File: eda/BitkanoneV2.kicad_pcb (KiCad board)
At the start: 2 copper layers, 0 parts

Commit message: WS2812B grid finished
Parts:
- added C401: 220u, Capacitor_SMD:CP_Elec_6.3x5.3, F.Cu at (273.8, 116.9)
- added C402: 220u, Capacitor_SMD:CP_Elec_6.3x5.3, F.Cu at (273.8, 109.7)
- added C900: 220u, Capacitor_SMD:CP_Elec_6.3x5.3, F.Cu at (53.0, 125.0)
- added C901: 100nF, Capacitor_SMD:C_0603_1608Metric, F.Cu at (32.0, 27.0)
- added C902: 100nF, Capacitor_SMD:C_0603_1608Metric, F.Cu at (46.0, 27.0)
- added C903: 100nF, Capacitor_SMD:C_0603_1608Metric, F.Cu at (60.0, 27.0)
- added C904: 100nF, Capacitor_SMD:C_0603_1608Metric, F.Cu at (74.0, 27.0)
- added C905: 100nF, Capacitor_SMD:C_0603_1608Metric, F.Cu at (88.0, 27.0)
- added C906: 100nF, Capacitor_SMD:C_0603_1608Metric, F.Cu at (102.0, 27.0)
- added C907: 100nF, Capacitor_SMD:C_0603_1608Metric, F.Cu at (116.0, 27.0)
- added C908: 100nF, Capacitor_SMD:C_0603_1608Metric, F.Cu at (32.0, 41.0)
- added C909: 100nF, Capacitor_SMD:C_0603_1608Metric, F.Cu at (46.0, 41.0)
- added C910: 100nF, Capacitor_SMD:C_0603_1608Metric, F.Cu at (60.0, 41.0)
- added C911: 100nF, Capacitor_SMD:C_0603_1608Metric, F.Cu at (74.0, 41.0)
- added C912: 100nF, Capacitor_SMD:C_0603_1608Metric, F.Cu at (88.0, 41.0)
- added C913: 100nF, Capacitor_SMD:C_0603_1608Metric, F.Cu at (102.0, 41.0)
- added C914: 100nF, Capacitor_SMD:C_0603_1608Metric, F.Cu at (116.0, 41.0)
- added C915: 100nF, Capacitor_SMD:C_0603_1608Metric, F.Cu at (32.0, 55.0)
- added C916: 100nF, Capacitor_SMD:C_0603_1608Metric, F.Cu at (46.0, 55.0)
- added C917: 100nF, Capacitor_SMD:C_0603_1608Metric, F.Cu at (60.0, 55.0)
- added C918: 100nF, Capacitor_SMD:C_0603_1608Metric, F.Cu at (74.0, 55.0)
- added C919: 100nF, Capacitor_SMD:C_0603_1608Metric, F.Cu at (81.1, 48.6)
- added C920: 100nF, Capacitor_SMD:C_0603_1608Metric, F.Cu at (102.0, 55.0)
- added C921: 100nF, Capacitor_SMD:C_0603_1608Metric, F.Cu at (116.0, 55.0)
- added C922: 100nF, Capacitor_SMD:C_0603_1608Metric, F.Cu at (32.0, 69.0)
- added C923: 100nF, Capacitor_SMD:C_0603_1608Metric, F.Cu at (46.0, 69.0)
- added C924: 100nF, Capacitor_SMD:C_0603_1608Metric, F.Cu at (60.0, 69.0)
- added C925: 100nF, Capacitor_SMD:C_0603_1608Metric, F.Cu at (74.0, 69.0)
- added C926: 100nF, Capacitor_SMD:C_0603_1608Metric, F.Cu at (88.0, 69.0)
- added C927: 100nF, Capacitor_SMD:C_0603_1608Metric, F.Cu at (102.0, 69.0)
- added C928: 100nF, Capacitor_SMD:C_0603_1608Metric, F.Cu at (116.0, 69.0)
- added C929: 100nF, Capacitor_SMD:C_0603_1608Metric, F.Cu at (32.0, 83.0)
- added C930: 100nF, Capacitor_SMD:C_0603_1608Metric, F.Cu at (46.0, 83.0)
- added C931: 100nF, Capacitor_SMD:C_0603_1608Metric, F.Cu at (60.0, 83.0)
- added C932: 100nF, Capacitor_SMD:C_0603_1608Metric, F.Cu at (74.0, 83.0)
- added C933: 100nF, Capacitor_SMD:C_0603_1608Metric, F.Cu at (88.0, 83.0)
- added C934: 100nF, Capacitor_SMD:C_0603_1608Metric, F.Cu at (102.0, 83.0)
- added C935: 100nF, Capacitor_SMD:C_0603_1608Metric, F.Cu at (116.0, 83.0)
- added C936: 100nF, Capacitor_SMD:C_0603_1608Metric, F.Cu at (32.0, 97.0)
- added C937: 100nF, Capacitor_SMD:C_0603_1608Metric, F.Cu at (46.3, 97.0)
- added C938: 100nF, Capacitor_SMD:C_0603_1608Metric, F.Cu at (60.0, 97.0)
- added C939: 100nF, Capacitor_SMD:C_0603_1608Metric, F.Cu at (74.0, 97.0)
- added C940: 100nF, Capacitor_SMD:C_0603_1608Metric, F.Cu at (88.0, 97.0)
- added C941: 100nF, Capacitor_SMD:C_0603_1608Metric, F.Cu at (102.0, 97.0)
- added C942: 100nF, Capacitor_SMD:C_0603_1608Metric, F.Cu at (116.0, 97.0)
- added C943: 100nF, Capacitor_SMD:C_0603_1608Metric, F.Cu at (32.0, 111.0)
- added C944: 100nF, Capacitor_SMD:C_0603_1608Metric, F.Cu at (46.3, 111.0)
- added C945: 100nF, Capacitor_SMD:C_0603_1608Metric, F.Cu at (60.0, 111.0)
- added C946: 100nF, Capacitor_SMD:C_0603_1608Metric, F.Cu at (74.0, 111.0)
- added C947: 100nF, Capacitor_SMD:C_0603_1608Metric, F.Cu at (88.0, 111.0)
- added C948: 100nF, Capacitor_SMD:C_0603_1608Metric, F.Cu at (102.0, 111.0)
- added C949: 100nF, Capacitor_SMD:C_0603_1608Metric, F.Cu at (116.0, 111.0)
- added D901: WS2812B, LED_SMD:LED_WS2812B_PLCC4_5.0x5.0mm_P3.2mm, F.Cu at (27.0, 27.0)
- added D902: WS2812B, LED_SMD:LED_WS2812B_PLCC4_5.0x5.0mm_P3.2mm, F.Cu at (41.0, 27.0)
- added D903: WS2812B, LED_SMD:LED_WS2812B_PLCC4_5.0x5.0mm_P3.2mm, F.Cu at (55.0, 27.0)
- added D904: WS2812B, LED_SMD:LED_WS2812B_PLCC4_5.0x5.0mm_P3.2mm, F.Cu at (69.0, 27.0)
- added D905: WS2812B, LED_SMD:LED_WS2812B_PLCC4_5.0x5.0mm_P3.2mm, F.Cu at (83.0, 27.0)
- added D906: WS2812B, LED_SMD:LED_WS2812B_PLCC4_5.0x5.0mm_P3.2mm, F.Cu at (97.0, 27.0)
- added D907: WS2812B, LED_SMD:LED_WS2812B_PLCC4_5.0x5.0mm_P3.2mm, F.Cu at (111.0, 27.0)
- added D908: WS2812B, LED_SMD:LED_WS2812B_PLCC4_5.0x5.0mm_P3.2mm, F.Cu at (27.0, 41.0)
- added D909: WS2812B, LED_SMD:LED_WS2812B_PLCC4_5.0x5.0mm_P3.2mm, F.Cu at (41.0, 41.0)
- added D910: WS2812B, LED_SMD:LED_WS2812B_PLCC4_5.0x5.0mm_P3.2mm, F.Cu at (55.0, 41.0)
- added D911: WS2812B, LED_SMD:LED_WS2812B_PLCC4_5.0x5.0mm_P3.2mm, F.Cu at (69.0, 41.0)
- added D912: WS2812B, LED_SMD:LED_WS2812B_PLCC4_5.0x5.0mm_P3.2mm, F.Cu at (83.0, 41.0)
- added D913: WS2812B, LED_SMD:LED_WS2812B_PLCC4_5.0x5.0mm_P3.2mm, F.Cu at (97.0, 41.0)
- added D914: WS2812B, LED_SMD:LED_WS2812B_PLCC4_5.0x5.0mm_P3.2mm, F.Cu at (111.0, 41.0)
- added D915: WS2812B, LED_SMD:LED_WS2812B_PLCC4_5.0x5.0mm_P3.2mm, F.Cu at (27.0, 55.0)
- added D916: WS2812B, LED_SMD:LED_WS2812B_PLCC4_5.0x5.0mm_P3.2mm, F.Cu at (41.0, 55.0)
- added D917: WS2812B, LED_SMD:LED_WS2812B_PLCC4_5.0x5.0mm_P3.2mm, F.Cu at (55.0, 55.0)
- added D918: WS2812B, LED_SMD:LED_WS2812B_PLCC4_5.0x5.0mm_P3.2mm, F.Cu at (69.0, 55.0)
- added D919: WS2812B, LED_SMD:LED_WS2812B_PLCC4_5.0x5.0mm_P3.2mm, F.Cu at (83.0, 55.0)
- added D920: WS2812B, LED_SMD:LED_WS2812B_PLCC4_5.0x5.0mm_P3.2mm, F.Cu at (97.0, 55.0)
- added D921: WS2812B, LED_SMD:LED_WS2812B_PLCC4_5.0x5.0mm_P3.2mm, F.Cu at (111.0, 55.0)
- added D922: WS2812B, LED_SMD:LED_WS2812B_PLCC4_5.0x5.0mm_P3.2mm, F.Cu at (27.0, 69.0)
- added D923: WS2812B, LED_SMD:LED_WS2812B_PLCC4_5.0x5.0mm_P3.2mm, F.Cu at (41.0, 69.0)
- added D924: WS2812B, LED_SMD:LED_WS2812B_PLCC4_5.0x5.0mm_P3.2mm, F.Cu at (55.0, 69.0)
- added D925: WS2812B, LED_SMD:LED_WS2812B_PLCC4_5.0x5.0mm_P3.2mm, F.Cu at (69.0, 69.0)
- added D926: WS2812B, LED_SMD:LED_WS2812B_PLCC4_5.0x5.0mm_P3.2mm, F.Cu at (83.0, 69.0)
- added D927: WS2812B, LED_SMD:LED_WS2812B_PLCC4_5.0x5.0mm_P3.2mm, F.Cu at (97.0, 69.0)
- added D928: WS2812B, LED_SMD:LED_WS2812B_PLCC4_5.0x5.0mm_P3.2mm, F.Cu at (111.0, 69.0)
- added D929: WS2812B, LED_SMD:LED_WS2812B_PLCC4_5.0x5.0mm_P3.2mm, F.Cu at (27.0, 83.0)
- added D930: WS2812B, LED_SMD:LED_WS2812B_PLCC4_5.0x5.0mm_P3.2mm, F.Cu at (41.0, 83.0)
- added D931: WS2812B, LED_SMD:LED_WS2812B_PLCC4_5.0x5.0mm_P3.2mm, F.Cu at (55.0, 83.0)
- added D932: WS2812B, LED_SMD:LED_WS2812B_PLCC4_5.0x5.0mm_P3.2mm, F.Cu at (69.0, 83.0)
- added D933: WS2812B, LED_SMD:LED_WS2812B_PLCC4_5.0x5.0mm_P3.2mm, F.Cu at (83.0, 83.0)
- added D934: WS2812B, LED_SMD:LED_WS2812B_PLCC4_5.0x5.0mm_P3.2mm, F.Cu at (97.0, 83.0)
- added D935: WS2812B, LED_SMD:LED_WS2812B_PLCC4_5.0x5.0mm_P3.2mm, F.Cu at (111.0, 83.0)
- added D936: WS2812B, LED_SMD:LED_WS2812B_PLCC4_5.0x5.0mm_P3.2mm, F.Cu at (27.0, 97.0)
- added D937: WS2812B, LED_SMD:LED_WS2812B_PLCC4_5.0x5.0mm_P3.2mm, F.Cu at (41.0, 97.0)
- added D938: WS2812B, LED_SMD:LED_WS2812B_PLCC4_5.0x5.0mm_P3.2mm, F.Cu at (55.0, 97.0)
- added D939: WS2812B, LED_SMD:LED_WS2812B_PLCC4_5.0x5.0mm_P3.2mm, F.Cu at (69.0, 97.0)
- added D940: WS2812B, LED_SMD:LED_WS2812B_PLCC4_5.0x5.0mm_P3.2mm, F.Cu at (83.0, 97.0)
- added D941: WS2812B, LED_SMD:LED_WS2812B_PLCC4_5.0x5.0mm_P3.2mm, F.Cu at (97.0, 97.0)
- added D942: WS2812B, LED_SMD:LED_WS2812B_PLCC4_5.0x5.0mm_P3.2mm, F.Cu at (111.0, 97.0)
- added D943: WS2812B, LED_SMD:LED_WS2812B_PLCC4_5.0x5.0mm_P3.2mm, F.Cu at (27.0, 111.0)
- added D944: WS2812B, LED_SMD:LED_WS2812B_PLCC4_5.0x5.0mm_P3.2mm, F.Cu at (41.0, 111.0)
- added D945: WS2812B, LED_SMD:LED_WS2812B_PLCC4_5.0x5.0mm_P3.2mm, F.Cu at (55.0, 111.0)
- added D946: WS2812B, LED_SMD:LED_WS2812B_PLCC4_5.0x5.0mm_P3.2mm, F.Cu at (69.0, 111.0)
- added D947: WS2812B, LED_SMD:LED_WS2812B_PLCC4_5.0x5.0mm_P3.2mm, F.Cu at (83.0, 111.0)
- added D948: WS2812B, LED_SMD:LED_WS2812B_PLCC4_5.0x5.0mm_P3.2mm, F.Cu at (97.0, 111.0)
- added D949: WS2812B, LED_SMD:LED_WS2812B_PLCC4_5.0x5.0mm_P3.2mm, F.Cu at (111.0, 111.0)
- added J221: Jumper, Jumper:SolderJumper-2_P1.3mm_Open_Pad1.0x1.5mm, F.Cu at (280.3, 107.4)
- added J222: Jumper, Jumper:SolderJumper-2_P1.3mm_Open_Pad1.0x1.5mm, F.Cu at (249.0, 136.5)
- added J231: Jumper, Jumper:SolderJumper-2_P1.3mm_Open_Pad1.0x1.5mm, F.Cu at (252.4, 133.9)
- added J232: Jumper, Jumper:SolderJumper-2_P1.3mm_Open_Pad1.0x1.5mm, F.Cu at (249.0, 133.9)
- added J233: Jumper, Jumper:SolderJumper-2_P1.3mm_Open_Pad1.0x1.5mm, F.Cu at (153.0, 76.0)
- added J234: Jumper, Jumper:SolderJumper-2_P1.3mm_Open_Pad1.0x1.5mm, F.Cu at (255.7, 129.9)
- added R221: 1k8, Resistor_SMD:R_0603_1608Metric_Pad1.05x0.95mm_HandSolder, F.Cu at (225.7, 160.6)
- added R222: 1k8, Resistor_SMD:R_0603_1608Metric_Pad1.05x0.95mm_HandSolder, F.Cu at (249.0, 138.5)
- added U201: BluePill_STM32F103C, BluePill_breakouts:BluePill_STM32F103C, B.Cu at (92.4, 76.0)
- added U202: MCP2551-I-SN, Package_SO:SOIC-8_3.9x4.9mm_P1.27mm, F.Cu at (202.0, 83.0)
- added U301: 10DOF, Connector_PinSocket_2.54mm:PinSocket_1x08_P2.54mm_Vertical, F.Cu at (252.8, 108.0)
- added X101: 01x02M, Connector_PinHeader_2.54mm:PinHeader_1x02_P2.54mm_Vertical, F.Cu at (260.0, 127.2)
- added X200: 01x03M, Connector_PinHeader_2.54mm:PinHeader_1x03_P2.54mm_Vertical, F.Cu at (258.0, 125.0)
- added X201: 5VUSB, Jumper:SolderJumper-2_P1.3mm_Open_Pad1.0x1.5mm, F.Cu at (249.0, 129.9)
- added X211: Jumper, Jumper:SolderJumper-2_P1.3mm_Open_Pad1.0x1.5mm, F.Cu at (252.4, 128.8)
- added X222: Jumper, Jumper:SolderJumper-2_P1.3mm_Open_Pad1.0x1.5mm, F.Cu at (252.4, 131.4)
- added X231: Bus, Connector_PinSocket_2.54mm:PinSocket_1x05_P2.54mm_Vertical, F.Cu at (267.2, 108.0)
- added X232: Bus, Connector_PinSocket_2.54mm:PinSocket_1x05_P2.54mm_Vertical, F.Cu at (260.0, 108.0)
- added X233: Bus, Connector_PinSocket_2.54mm:PinSocket_1x05_P2.54mm_Vertical, F.Cu at (256.4, 108.0)
- added X234: Bus, Connector_PinSocket_2.54mm:PinSocket_1x05_P2.54mm_Vertical, F.Cu at (263.6, 108.0)
- added X401: MotorCon, Connector_PinSocket_2.54mm:PinSocket_1x08_P2.54mm_Vertical, F.Cu at (249.2, 108.0)
- added X990: Conn_01x01, Connector_PinHeader_2.54mm:PinHeader_1x01_P2.54mm_Vertical, F.Cu at (123.0, 34.0)

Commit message: placement finished
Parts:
- removed J221, J222, X211, X222: Jumper, Jumper:SolderJumper-2_P1.3mm_Open_Pad1.0x1.5mm
- added J211: JH23, Jumper:SolderJumper-3_P1.3mm_Open_RoundedPad1.0x1.5mm_NumberLabels, B.Cu at (98.2, 46.1)
- added J212: JL23, Jumper:SolderJumper-3_P1.3mm_Open_RoundedPad1.0x1.5mm_NumberLabels, B.Cu at (98.2, 50.0)
- U201: footprint BluePill_breakouts:BluePill_STM32F103C -> BluePill_breakouts:BluePill_STM32F103C_Center_NoPROG
- U301, X201, X401: moved to B.Cu
- moved X200 248.3 mm to (27.0, 34.0), turned to 90 degrees
- moved X234 245.5 mm to (22.0, 63.9)
- moved J234 244.1 mm to (22.0, 59.5), turned to 270 degrees
- moved X101 239.3 mm to (22.0, 102.7)
- moved J231 223.0 mm to (59.5, 22.0)
- moved X231 220.7 mm to (63.9, 22.0), turned to 90 degrees
- moved C401 202.3 mm to (73.2, 90.0)
- moved U301 194.8 mm to (58.8, 90.0), turned to 90 degrees
- moved X233 192.6 mm to (63.9, 116.0), turned to 90 degrees
- moved C402 187.6 mm to (87.2, 90.0)
- moved R222 187.3 mm to (84.0, 50.0)
- moved R221 182.2 mm to (84.0, 46.1)
- moved X201 176.3 mm to (89.3, 55.0)
- moved X401 159.2 mm to (90.0, 104.0), turned to 90 degrees
- moved J232 152.4 mm to (116.0, 59.5), turned to 270 degrees
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
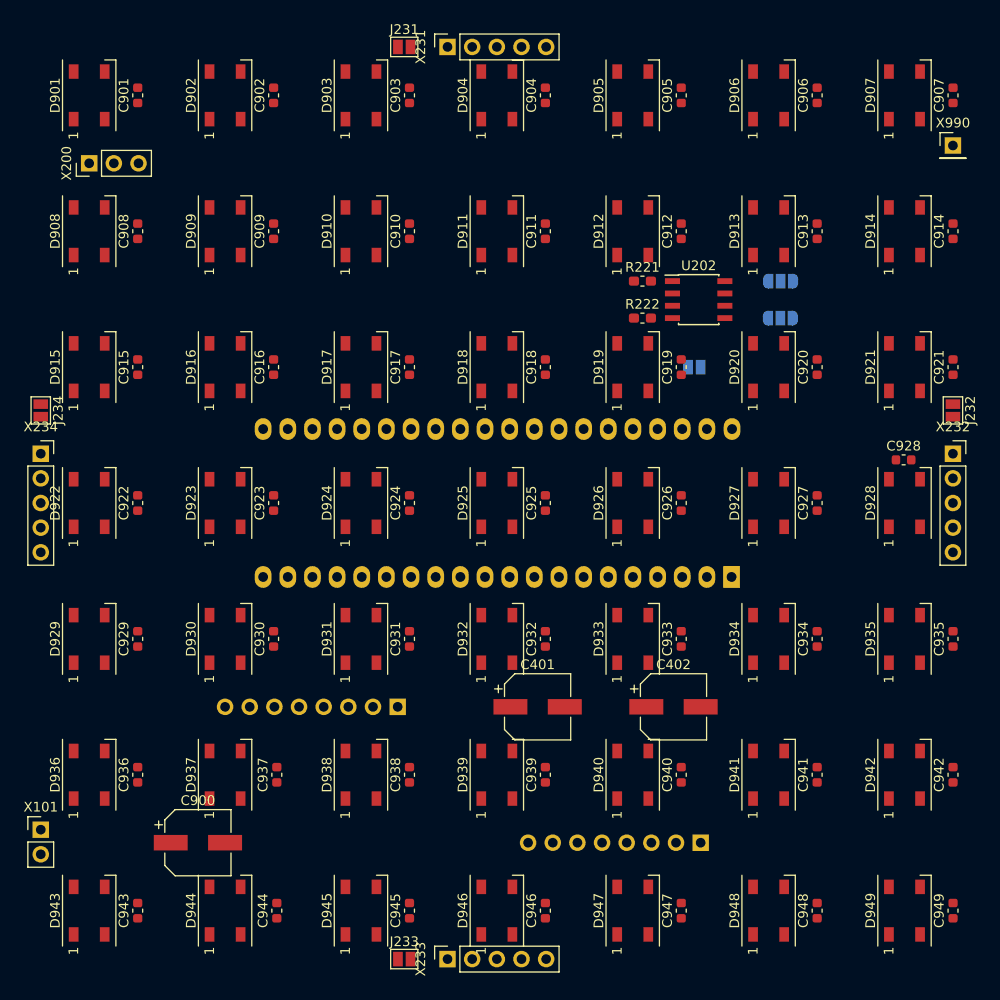
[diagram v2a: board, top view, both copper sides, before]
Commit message: all but bus routed
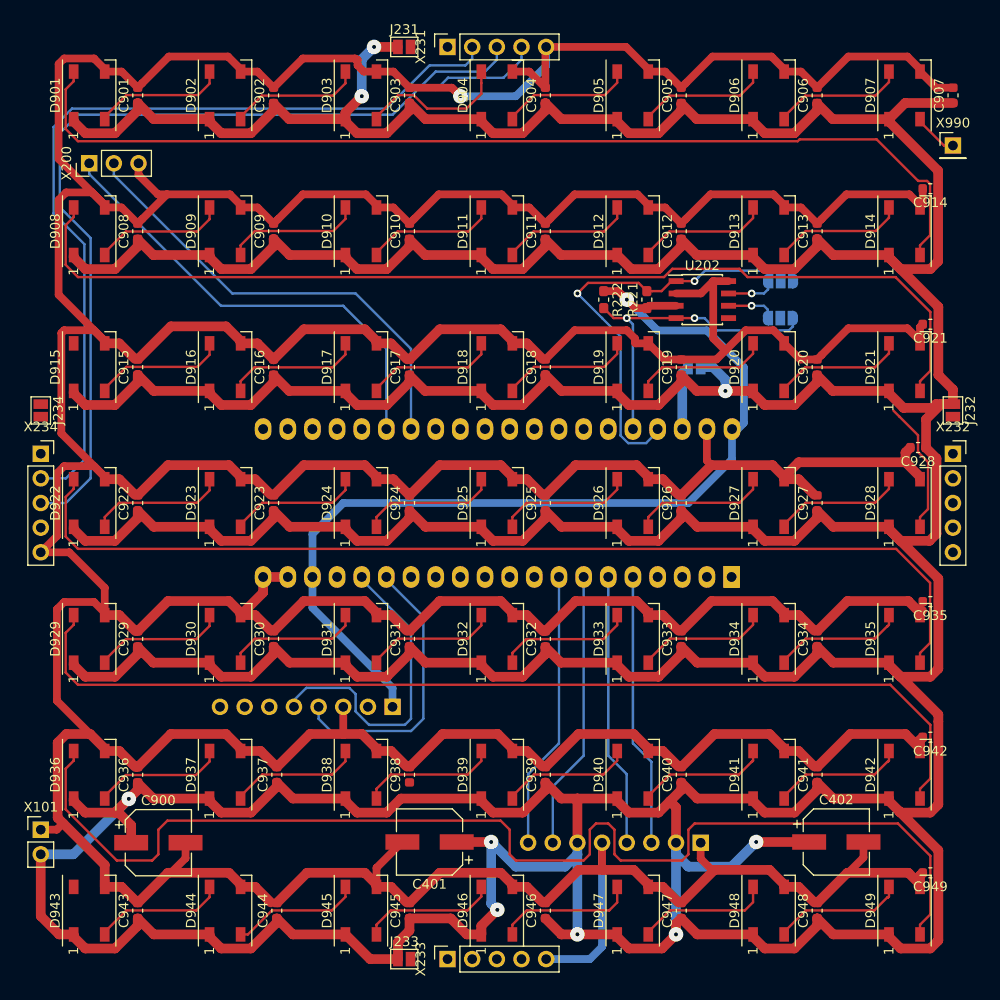
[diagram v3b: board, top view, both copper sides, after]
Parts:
- moved C402 21.8 mm to (104.0, 103.9)
- moved C401 17.8 mm to (62.1, 103.9), turned to 180 degrees
- moved C921 4.99 mm to (113.7, 50.6), turned to 180 degrees
- moved C914 4.97 mm to (113.7, 36.6), turned to 180 degrees
- moved C949 4.55 mm to (113.7, 107.1), turned to 180 degrees
- moved C942 4.52 mm to (113.7, 93.1), turned to 180 degrees
- moved C935 4.49 mm to (113.7, 79.2), turned to 180 degrees
- moved R222 4.42 mm to (80.0, 48.0), turned to 270 degrees
- moved C900 4.07 mm to (34.1, 104.0)
- moved R221 1.96 mm to (84.5, 48.0), turned to 90 degrees
- moved C928 1.95 mm to (112.4, 63.3), turned to 180 degrees
- moved U301 0.52 mm to (58.3, 90.0)
- moved U202 0.38 mm to (90.2, 48.0)
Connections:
- net Net-(J211-Pad2) renamed /CANH
- net Net-(J212-Pad2) renamed /CANL
- X101 pad 1: +5V -> GND
- X101 pad 2: GND -> +5V
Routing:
- net +5V: track 0.00 -> 964.9 mm, vias 0 -> 9
- net GND: track 0.00 -> 930.0 mm, vias 0 -> 1
- net Net-(D936-Pad4): track 0.00 -> 123.4 mm
- net Net-(D908-Pad4): track 0.00 -> 106.6 mm
- net Net-(D922-Pad4): track 0.00 -> 105.9 mm
- net Net-(D929-Pad4): track 0.00 -> 105.6 mm
- net Net-(D901-Pad4): track 0.00 -> 105.6 mm
- net +3V3: track 0.00 -> 101.5 mm, vias 0 -> 1
- net /CANL: track 0.00 -> 92.5 mm
- net /CANH: track 0.00 -> 88.1 mm
- net Net-(U201-Pad27): track 0.00 -> 47.5 mm
- net Net-(U201-Pad26): track 0.00 -> 47.4 mm
- net /CANTX: track 0.00 -> 46.2 mm, vias 0 -> 2
- net /CANRX: track 0.00 -> 33.2 mm, vias 0 -> 2
- net /SENS_SDA: track 0.00 -> 32.9 mm
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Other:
- net class Supply added: clearance 0.2, trace_width 1, via_dia 1.5, via_drill 0.4
- net class SupplySM added: clearance 0.2, trace_width 0.8, via_dia 1.5, via_drill 0.4

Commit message: routing finished
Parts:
- added X991: Conn_01x01, Connector_PinHeader_2.54mm:PinHeader_1x01_P2.54mm_Vertical, F.Cu at (116.0, 32.2)
- moved X990 115.5 mm to (26.5, 105.2)
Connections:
- U201 pad 10: Net-(U201-Pad10) -> /TRight
- U201 pad 12: Net-(U201-Pad12) -> /TBottom
- U201 pad 21: /TRight -> /TLeft
- U201 pad 22: /TTop -> Net-(U201-Pad22)
- U201 pad 23: /TLeft -> Net-(U201-Pad23)
- U201 pad 25: /TBottom -> Net-(U201-Pad25)
- U201 pad 30: Net-(U201-Pad30) -> /TTop
- X990 pad 1: /LedGrid/DOUT -> /DIN
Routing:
- net /CANH: track 88.1 -> 287.3 mm, vias 0 -> 4
- net /CANL: track 92.5 -> 278.7 mm
- net Net-(D915-Pad4): track 14.0 -> 104.9 mm, vias 0 -> 2
- net /DIN: track 0.00 -> 59.9 mm
- net /TRight: track 0.00 -> 48.6 mm
- net /TBottom: track 0.00 -> 43.1 mm
- net /TTop: track 11.5 -> 48.5 mm, vias 0 -> 2
- net /TLeft: track 0.00 -> 28.2 mm
- net GND: track 930.0 -> 942.6 mm, vias 1 -> 2
- net +5V: track 964.9 -> 976.8 mm, vias 9 -> 11
- net Net-(J234-Pad2): track 0.00 -> 3.81 mm
- net Net-(J233-Pad2): track 0.00 -> 3.81 mm
- net Net-(J232-Pad2): track 0.00 -> 3.81 mm
- net Net-(J231-Pad2): track 0.00 -> 3.81 mm
- net Net-(J212-Pad3): track 5.08 -> 4.57 mm

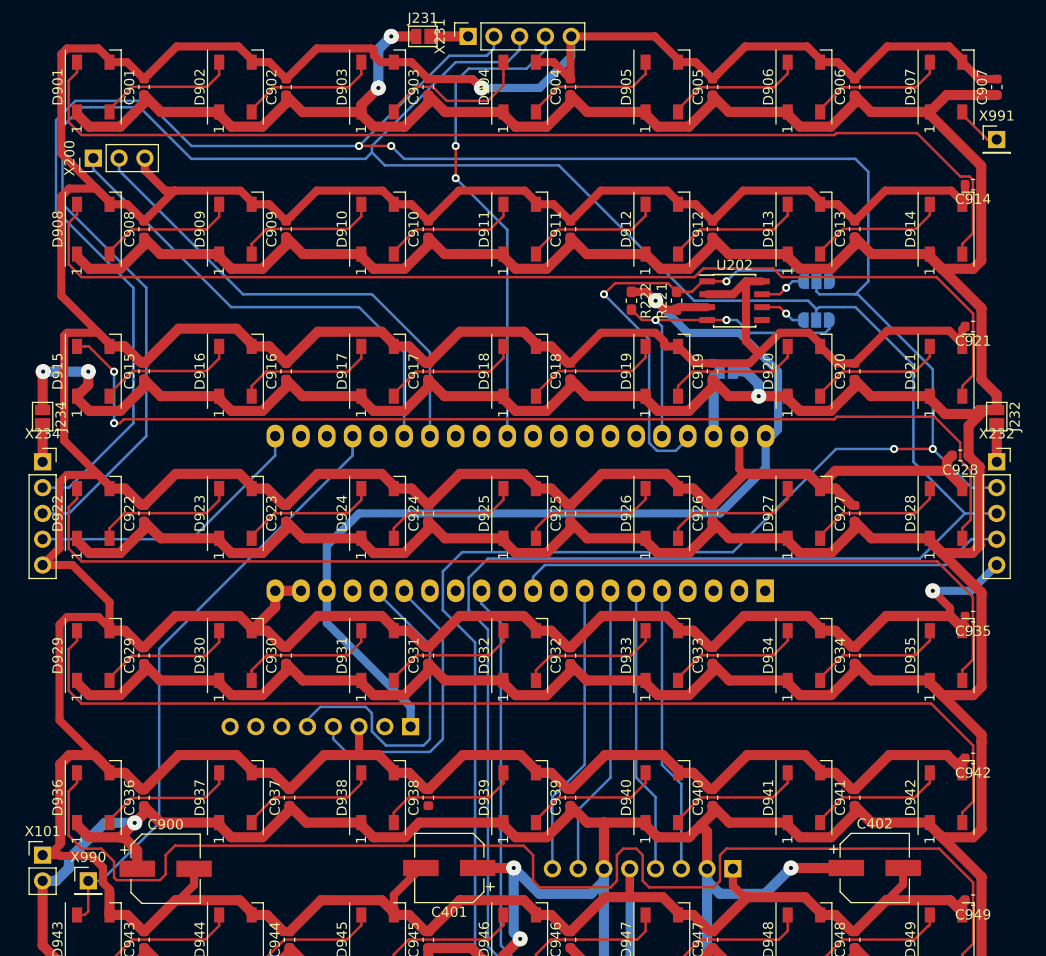
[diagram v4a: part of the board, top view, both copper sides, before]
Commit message: U301:more space; Phototransistors, Buttons and X42 added
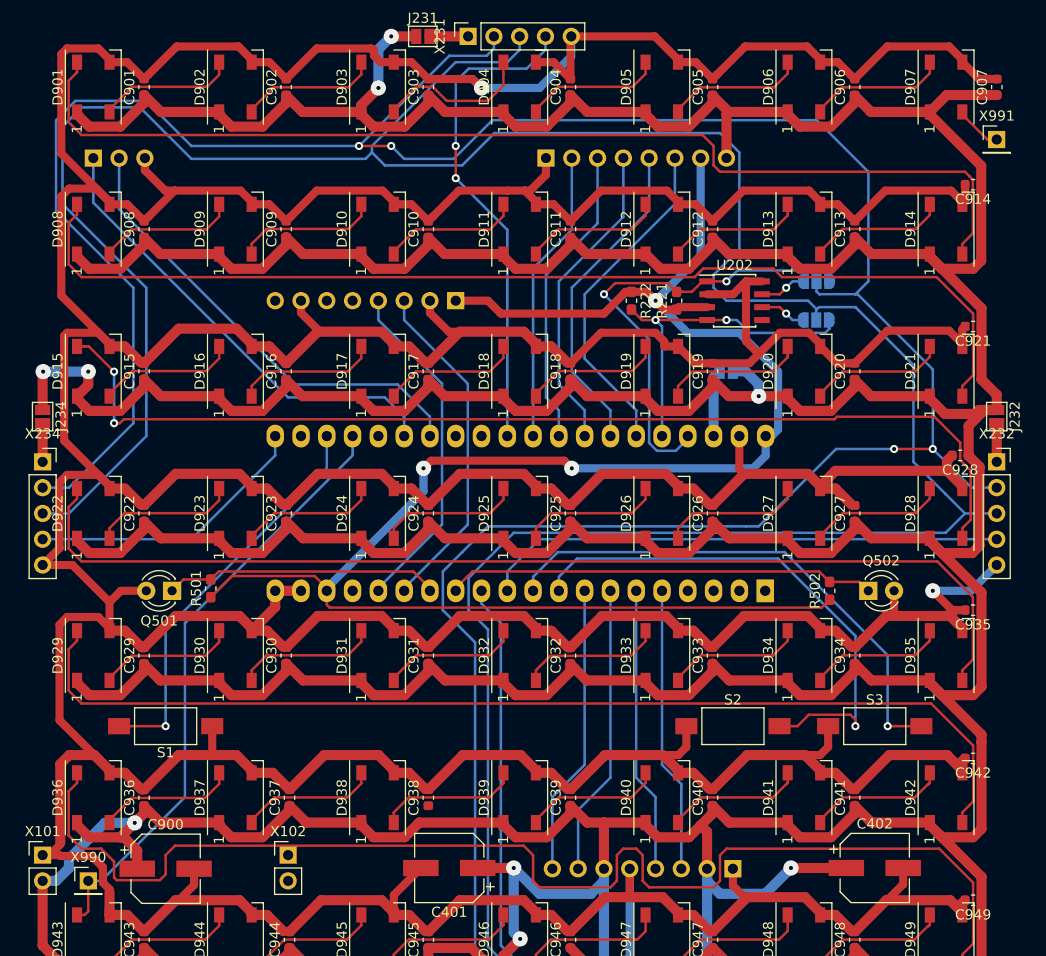
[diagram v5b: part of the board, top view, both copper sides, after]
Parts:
- added Q501: PH_NPN, LED_THT:LED_D3.0mm, F.Cu at (34.8, 76.6)
- added Q502: PH_NPN, LED_THT:LED_D3.0mm, F.Cu at (103.3, 76.6)
- added R501: 1k8, Resistor_SMD:R_0603_1608Metric_Pad1.05x0.95mm_HandSolder, F.Cu at (38.6, 76.4)
- added R502: 1k8, Resistor_SMD:R_0603_1608Metric_Pad1.05x0.95mm_HandSolder, F.Cu at (99.5, 76.6)
- added S1: SW, Button_Switch_SMD:SW_SPST_FSMSM, F.Cu at (34.1, 90.0)
- added S2: SW, Button_Switch_SMD:SW_SPST_FSMSM, F.Cu at (90.0, 90.0)
- added S3: SW, Button_Switch_SMD:SW_SPST_FSMSM, F.Cu at (104.0, 90.0)
- added X102: 01x02M, Connector_PinHeader_2.54mm:PinHeader_1x02_P2.54mm_Vertical, F.Cu at (46.2, 102.7)
- added X42: Conn_01x07_Male, Connector_PinSocket_2.54mm:PinSocket_1x08_P2.54mm_Vertical, B.Cu at (71.6, 34.0)
- U301: value 10DOF -> 6DOF
- X200: moved to B.Cu
- moved U301 42.2 mm to (62.7, 48.0)
- moved C935 0.63 mm to (113.7, 78.5)
- turned X200 to 270 degrees
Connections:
- U201 pad 10: /TRight -> Net-(S3-Pad2)
- U201 pad 11: Net-(U201-Pad11) -> /TRight
- U201 pad 13: Net-(U201-Pad13) -> /Photo2
- U201 pad 14: Net-(U201-Pad14) -> /Photo1
- U201 pad 31: Net-(U201-Pad31) -> /X42_PB3
- U201 pad 32: Net-(U201-Pad32) -> /X42_PB4
- U201 pad 33: Net-(U201-Pad33) -> /X42_PB5
- U201 pad 34: Net-(U201-Pad34) -> /X42_SCL
- U201 pad 35: Net-(U201-Pad35) -> /X42_SDA
- U301 pad 2: Net-(U301-Pad2) -> GND
- U301 pad 3: GND -> /SENS_SCL
- U301 pad 4: /SENS_SCL -> /SENS_SDA
- U301 pad 5: /SENS_SDA -> Net-(U301-Pad5)
- U301 pad 7: Net-(U301-Pad7) -> GND
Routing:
- net +3V3: track 101.5 -> 183.5 mm, vias 1 -> 3
- net Net-(S2-Pad2): track 0.00 -> 52.2 mm, vias 0 -> 1
- net Net-(S3-Pad2): track 0.00 -> 51.8 mm, vias 0 -> 1
- net /Photo2: track 0.00 -> 42.4 mm
- net Net-(S1-Pad2): track 0.00 -> 39.7 mm, vias 0 -> 1
- net /X42_SDA: track 0.00 -> 33.2 mm
- net /X42_SCL: track 0.00 -> 32.1 mm
- net /X42_PB5: track 0.00 -> 31.1 mm
- net GND: track 942.6 -> 973.1 mm
- net /X42_PB4: track 0.00 -> 30.0 mm
- net /X42_PB3: track 0.00 -> 29.0 mm
- net /Photo1: track 0.00 -> 27.1 mm
- net /CANL: track 278.7 -> 292.7 mm
- net /SENS_SCL: track 29.3 -> 34.0 mm
- net +5V: track 976.8 -> 981.4 mm
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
